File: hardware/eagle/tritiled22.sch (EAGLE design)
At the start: 15 parts

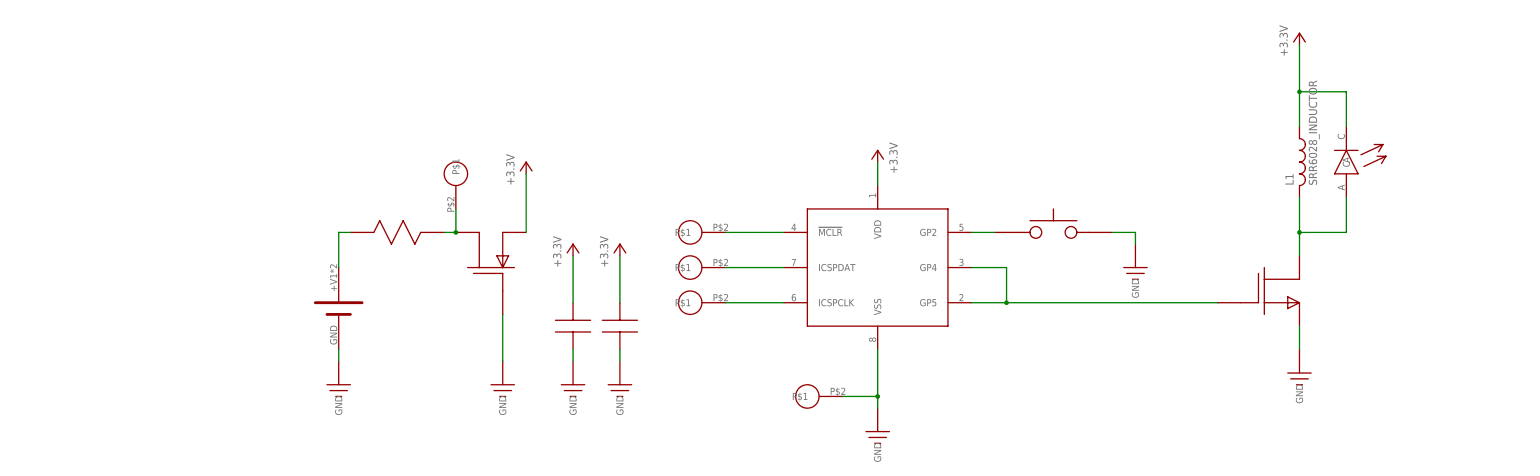
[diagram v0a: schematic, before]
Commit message: added names and values to schematic and PCB
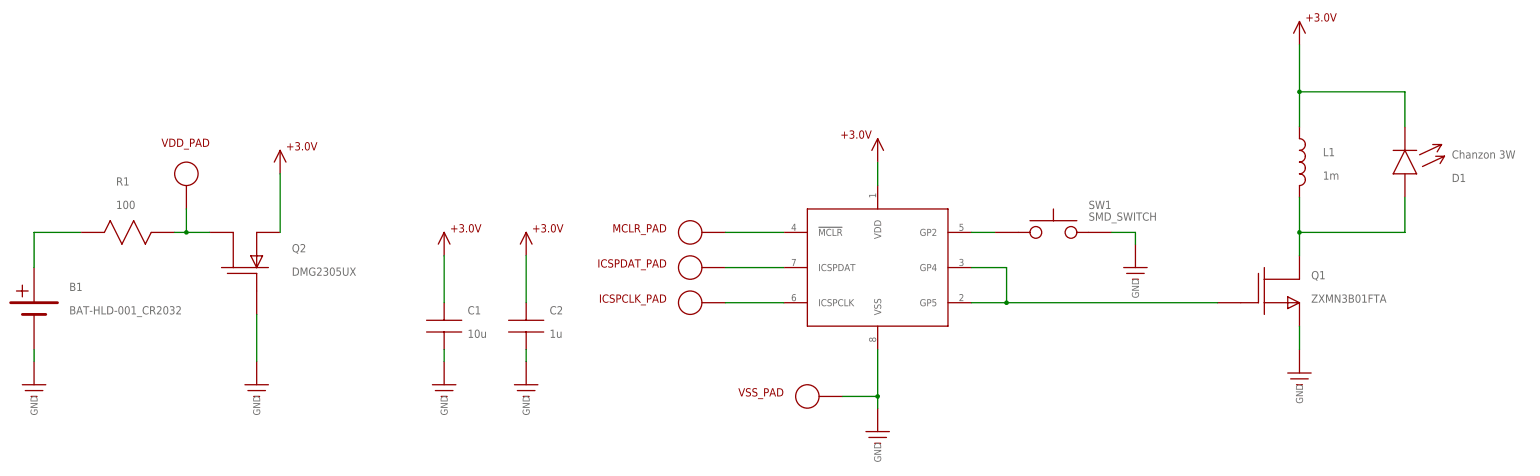
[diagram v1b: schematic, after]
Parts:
- removed U$12: LED_3W, tritiled:LED_3W
- removed U$17: R, tritiled:R
- removed U$22: DMG2305UXSOT23, tritiled:DMG2305UXSOT23
- removed U$24: C1206, tritiled:C1206
- removed U$25: C0805, tritiled:C0805
- removed U$6: BAT-HLD-001_CR2032, tritiled:BAT-HLD-001_CR2032
- added B1: BAT-HLD-001_CR2032, tritiled:BAT-HLD-001_CR2032
- added C1: 10u, tritiled:C1206
- added C2: 1u, tritiled:C0805
- added D1: Chanzon 3W, tritiled:LED_3W
- added Q2: DMG2305UX, tritiled:DMG2305UXSOT23
- added R1: 100, tritiled:R1206
- L1: value SRR6028_INDUCTOR -> 1m
- Q1: value ZXMN3B01FSOT23 -> ZXMN3B01FTA
- renumbered U$1 to U1, U$16 to Q1, U$9 to SW1
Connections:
- net +3.3V: now also C1.P$1, C2.P$1, D1.C, Q2.S; no longer U$12.C, U$22.S, U$24.P$1, U$25.P$1
- net GND: now also B1.0V, C1.P$2, C2.P$2, Q2.G; no longer U$22.G, U$24.P$2, U$25.P$2, U$6.0V
- net N$5: now also D1.A; no longer U$12.A
- net VBATT: now also B1.+V, R1.P$1; no longer U$17.P$1, U$6.+V
- net VSAFE: now also Q2.D, R1.P$2; no longer U$17.P$2, U$22.D
